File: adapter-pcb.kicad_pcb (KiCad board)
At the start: 4 copper layers, 90.2 x 95.9 mm, 7 parts, among them J3 SS5-80-3.50-X-D-K-XX, M1 MountingHole_Pad_MP, M2 MountingHole_Pad_MP, M3 MountingHole_Pad_MP, M4 MountingHole_Pad_MP

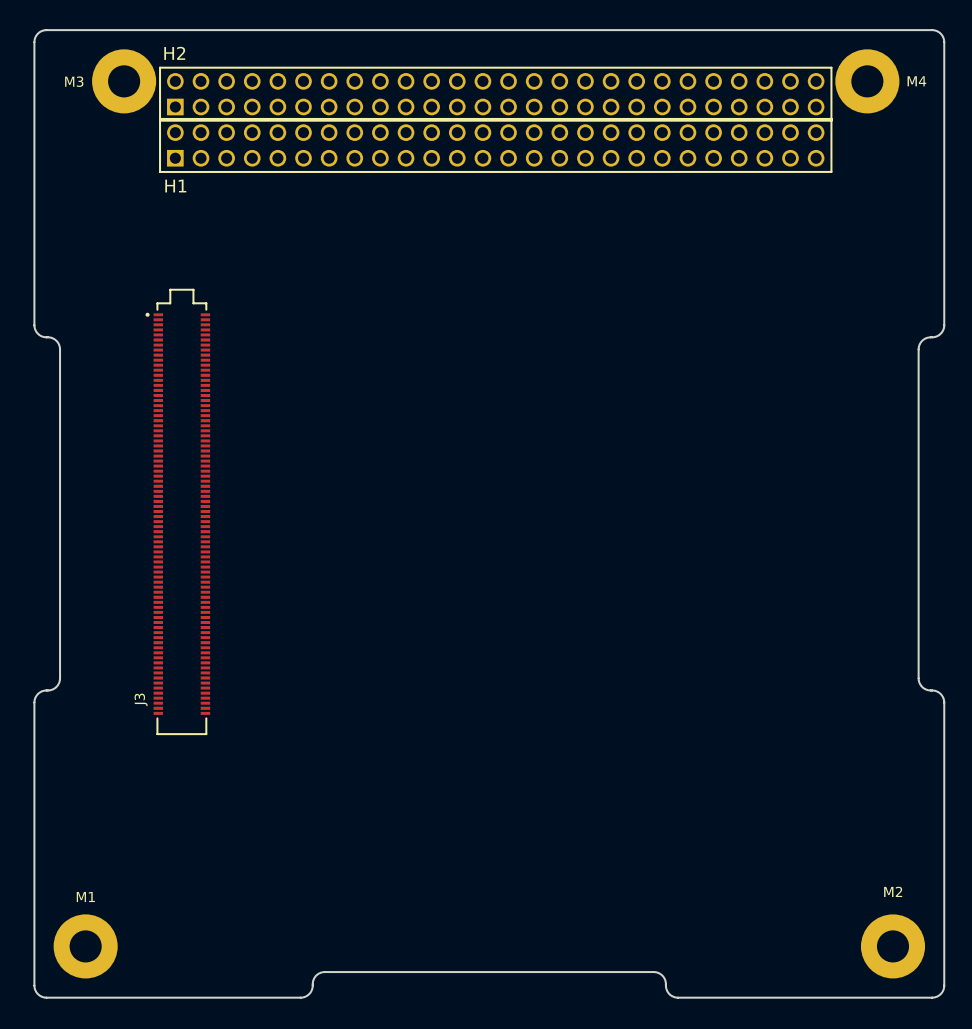
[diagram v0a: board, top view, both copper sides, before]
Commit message: Routed PCB (with I2C buffer)
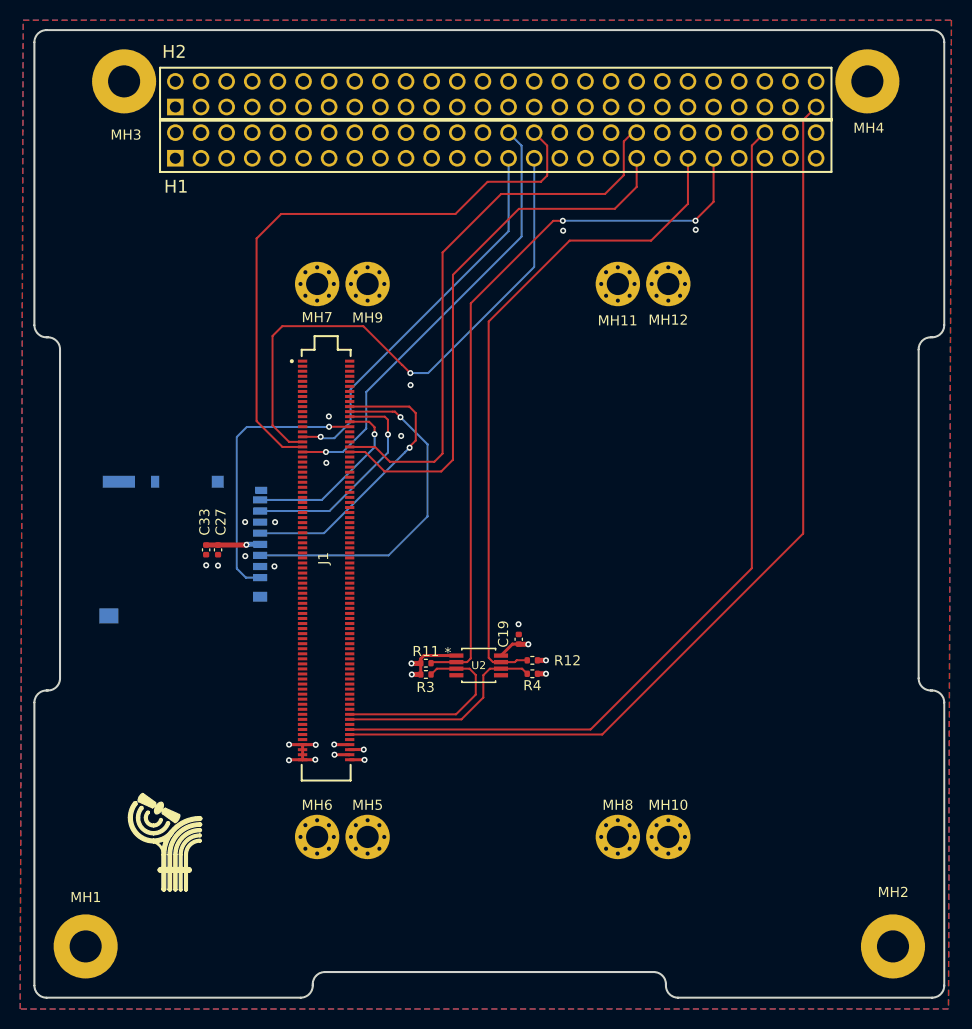
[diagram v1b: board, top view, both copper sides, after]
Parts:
- removed J3: SS5-80-3.50-X-D-K-XX, adapter:SAMTEC_SS5-80-3.50-X-D-K-XX
- added C19: 10n, Capacitor_SMD:C_0402_1005Metric, F.Cu at (153.4, 106.9)
- added C27: 100n, Capacitor_SMD:C_0402_1005Metric, F.Cu at (123.6, 98.0)
- added C33: 1u, Capacitor_SMD:C_0402_1005Metric, F.Cu at (122.4, 98.0)
- added J1: SS5-80-3.50-X-D-K-XX, adapter:SAMTEC_SS5-80-3.50-X-D-K-XX, F.Cu at (134.3, 99.1)
- added J2: DM3BT-DSF-PEJS, adapter:DM3BT_DSF_PEJS, B.Cu at (120.0, 98.0)
- added MH10: MountingHole_Pad_MP, MountingHole:MountingHole_2.2mm_M2_Pad_Via, F.Cu at (168.2, 126.5)
- added MH11: MountingHole_Pad_MP, MountingHole:MountingHole_2.2mm_M2_Pad_Via, F.Cu at (163.2, 71.7)
- added MH12: MountingHole_Pad_MP, MountingHole:MountingHole_2.2mm_M2_Pad_Via, F.Cu at (168.2, 71.7)
- added MH5: MountingHole_Pad_MP, MountingHole:MountingHole_2.2mm_M2_Pad_Via, F.Cu at (138.4, 126.5)
- added MH6: MountingHole_Pad_MP, MountingHole:MountingHole_2.2mm_M2_Pad_Via, F.Cu at (133.4, 126.5)
- added MH7: MountingHole_Pad_MP, MountingHole:MountingHole_2.2mm_M2_Pad_Via, F.Cu at (133.4, 71.7)
- added MH8: MountingHole_Pad_MP, MountingHole:MountingHole_2.2mm_M2_Pad_Via, F.Cu at (163.2, 126.5)
- added MH9: MountingHole_Pad_MP, MountingHole:MountingHole_2.2mm_M2_Pad_Via, F.Cu at (138.4, 71.7)
- added R11: 10K, Resistor_SMD:R_0402_1005Metric, F.Cu at (144.2, 109.2)
- added R12: 10K, Resistor_SMD:R_0402_1005Metric, F.Cu at (154.8, 109.0)
- added R3: 10K, Resistor_SMD:R_0402_1005Metric, F.Cu at (144.2, 110.4)
- added R4: 10K, Resistor_SMD:R_0402_1005Metric, F.Cu at (154.8, 110.3)
- added U2: LTC4300A-1IMS8_PBF, adapter:LTC4300A-1IMS8_PBF, F.Cu at (149.4, 109.5)
- renumbered M1 to MH1, M2 to MH2, M3 to MH3, M4 to MH4
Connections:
- H1 pad 21: I2C_SDA(2) -> unconnected-(H1-Pin_21-Pad21)
- H1 pad 23: I2C_SCL(2) -> unconnected-(H1-Pin_23-Pad23)
- H1 pad 27: unconnected-(H1-Pin_27-Pad27) -> MOSI
- H1 pad 28: unconnected-(H1-Pin_28-Pad28) -> SS/CS
- H1 pad 29: unconnected-(H1-Pin_29-Pad29) -> MISO
- H1 pad 30: unconnected-(H1-Pin_30-Pad30) -> SCLK
- H1 pad 37: unconnected-(H1-Pin_37-Pad37) -> UART_TX
- H1 pad 38: unconnected-(H1-Pin_38-Pad38) -> UART_RX
- H1 pad 41: unconnected-(H1-Pin_41-Pad41) -> I2C_SDA_CSKB
- H1 pad 43: unconnected-(H1-Pin_43-Pad43) -> I2C_SCL_CSKB
- H1 pad 48: unconnected-(H1-Pin_48-Pad48) -> SNN Enable
- H2 pad 13: unconnected-(H2-Pin_13-Pad13) -> +5V
- H2 pad 15: unconnected-(H2-Pin_15-Pad15) -> +5V
- H2 pad 16: unconnected-(H2-Pin_16-Pad16) -> +5V
- H2 pad 18: unconnected-(H2-Pin_18-Pad18) -> +3V3
- H2 pad 19: unconnected-(H2-Pin_19-Pad19) -> +3V3
- H2 pad 20: unconnected-(H2-Pin_20-Pad20) -> +3V3
- H2 pad 27: +3V3 -> unconnected-(H2-Pin_27-Pad27)
- H2 pad 28: +3V3 -> unconnected-(H2-Pin_28-Pad28)
- H2 pad 51: unconnected-(H2-Pin_51-Pad51) -> RESESTREQ
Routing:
- net RESESTREQ: track 0.00 -> 96.0 mm
- net SNN Enable: track 0.00 -> 90.2 mm
- net I2C_SCL_CSKB: track 0.00 -> 72.1 mm, vias 0 -> 2
- net I2C_SDA_CSKB: track 0.00 -> 66.5 mm
- net SCLK: track 0.00 -> 59.9 mm
- net UART_RX: track 0.00 -> 56.2 mm
- net MISO: track 0.00 -> 55.9 mm, vias 0 -> 1
- net UART_TX: track 0.00 -> 54.5 mm
- net SS/CS: track 0.00 -> 43.5 mm, vias 0 -> 1
- net MOSI: track 0.00 -> 38.1 mm, vias 0 -> 1
- net SD-CMD: track 0.00 -> 34.4 mm, vias 0 -> 1
- net SD-CCLK: track 0.00 -> 28.8 mm, vias 0 -> 1
- net SD-D2: track 0.00 -> 27.3 mm, vias 0 -> 1
- net +3V3: track 0.00 -> 23.2 mm, vias 0 -> 10
- net SD-D0: track 0.00 -> 22.2 mm, vias 0 -> 1
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- added copper zone on In2.Cu, net +3V3
- added copper zone on B.Cu, net GND
- added copper zone on F.Cu, net GND
- added copper zone on In1.Cu, net GND

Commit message: fixed and labeled CSKB header, added 3D models
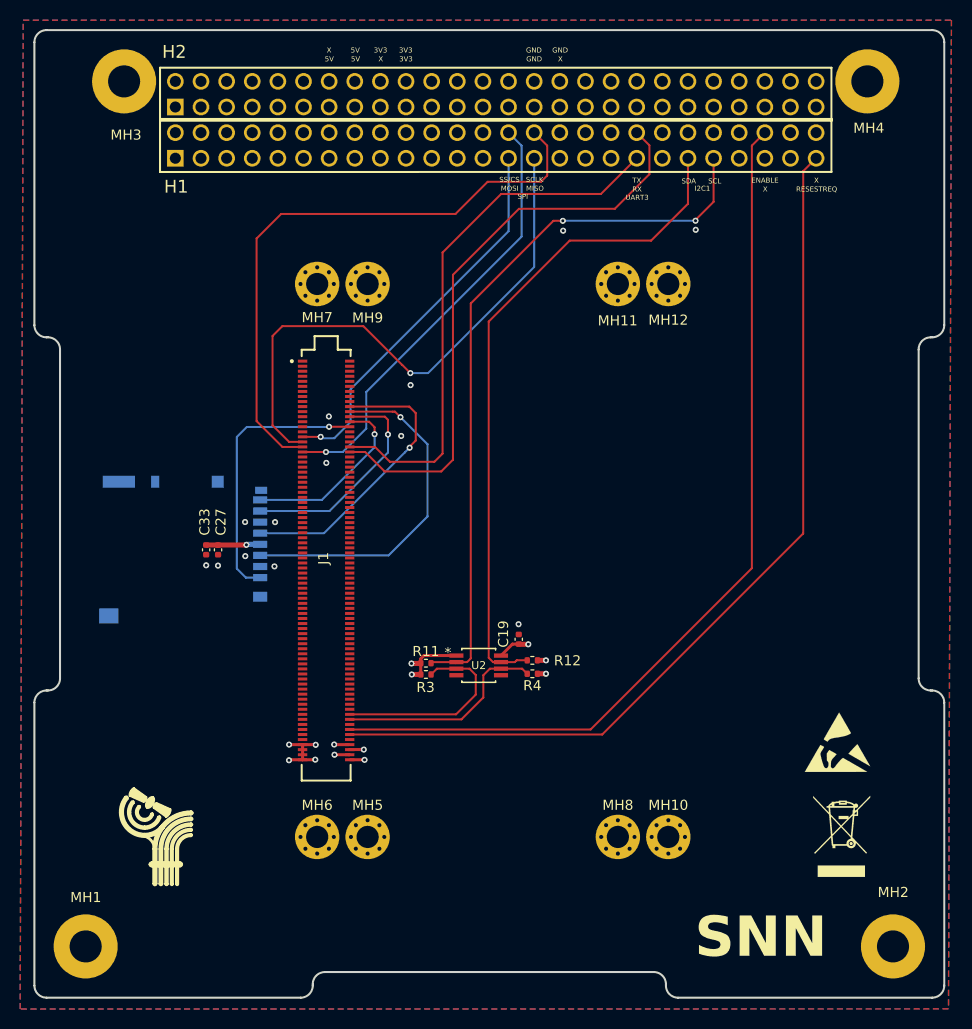
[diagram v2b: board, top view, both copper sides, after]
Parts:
- added REF**: ESD-Logo_6.6x6mm_SilkScreen, Symbol:ESD-Logo_6.6x6mm_SilkScreen, F.Cu at (185.0, 117.1)
- added REF**: WEEE-Logo_5.6x8mm_SilkScreen, Symbol:WEEE-Logo_5.6x8mm_SilkScreen, F.Cu at (185.4, 126.4)
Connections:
- H1 pad 37: UART_TX -> UART_RX
- H1 pad 38: UART_RX -> UART_TX
- H1 pad 51: unconnected-(H1-Pin_51-Pad51) -> RESESTREQ
- H2 pad 51: RESESTREQ -> unconnected-(H2-Pin_51-Pad51)
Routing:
- net RESESTREQ: track 96.0 -> 90.9 mm
- net UART_TX: track 54.5 -> 58.5 mm
- net UART_RX: track 56.2 -> 53.2 mm
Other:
- board text added: "3V3"
- board text added: "5V"
- board text added: "ENABLE"
- board text added: "GND"
- board text added: "I2C1"
- board text added: "MISO"
- board text added: "MOSI"
- board text added: "RESESTREQ"
- board text added: "RX"
- board text added: "SCL"
- board text added: "SCLK"
- board text added: "SDA"
- board text added: "SNN"
- board text added: "SPI"
- board text added: "SS/CS"
- board text added: "TX"
- board text added: "UART3"
- board text added: "X"

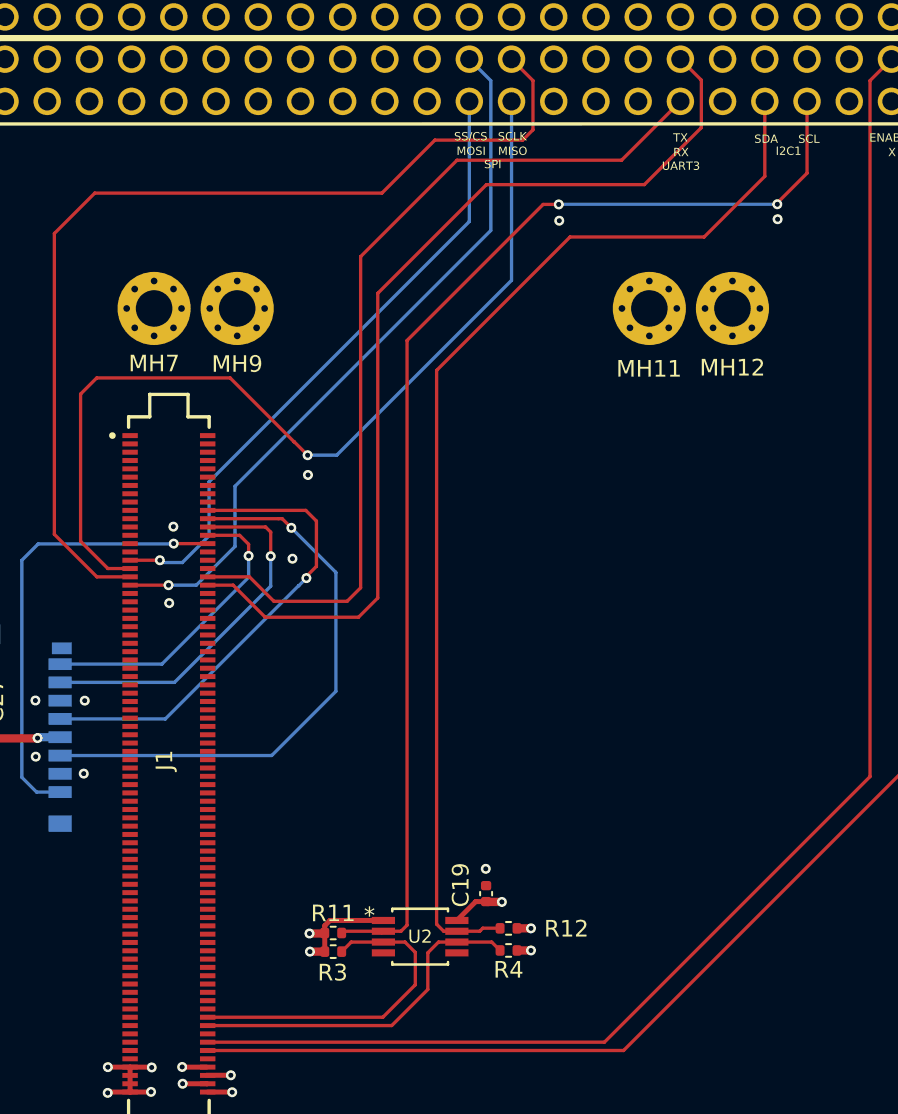
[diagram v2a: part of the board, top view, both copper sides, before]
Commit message: Fixed GND issues with connector and mounting holes
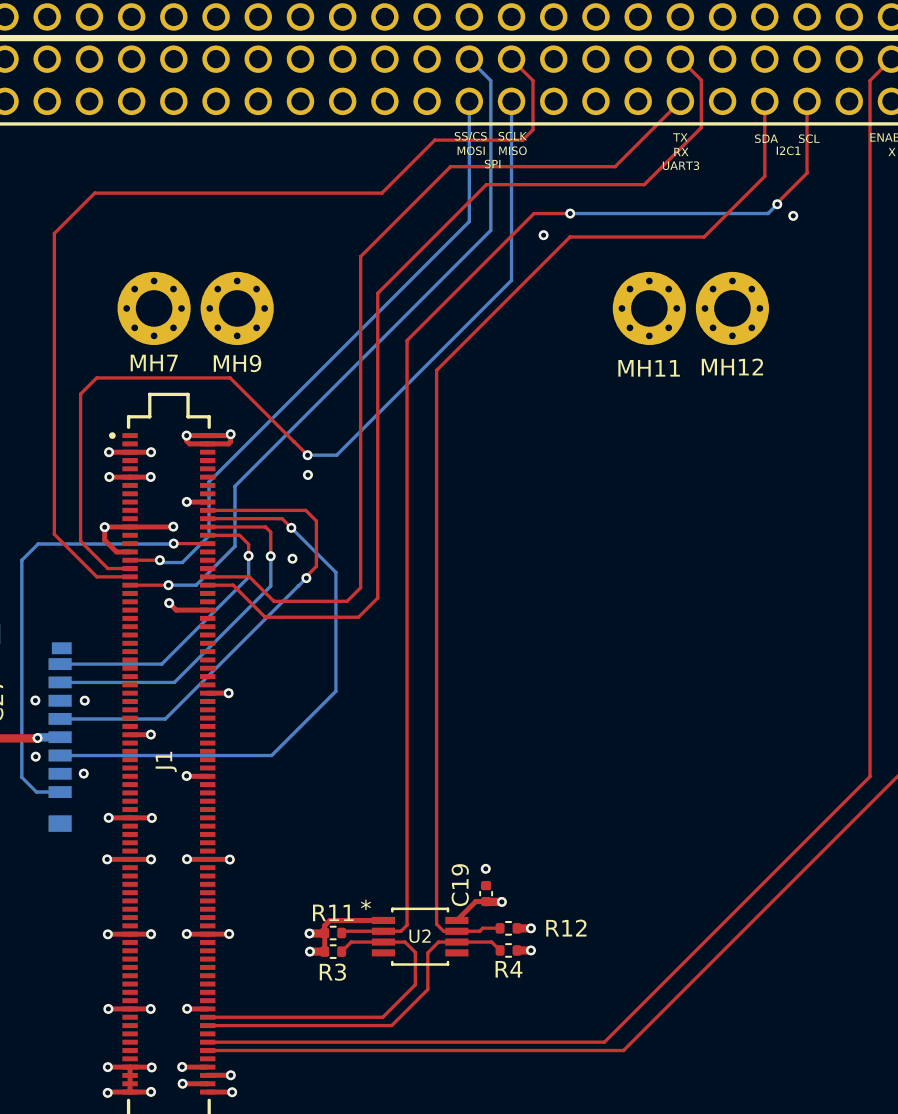
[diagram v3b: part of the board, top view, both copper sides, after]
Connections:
- MH10 pad 1: (no net) -> GND
- MH11 pad 1: (no net) -> GND
- MH12 pad 1: (no net) -> GND
- MH5 pad 1: (no net) -> GND
- MH6 pad 1: (no net) -> GND
- MH7 pad 1: (no net) -> GND
- MH8 pad 1: (no net) -> GND
- MH9 pad 1: (no net) -> GND
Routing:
- net GND: track 6.80 -> 49.1 mm, vias 17 -> 41
